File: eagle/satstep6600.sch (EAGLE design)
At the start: 42 parts, among them J3 STEPPER_CONN_2, T1 10K, U1 74HC123D

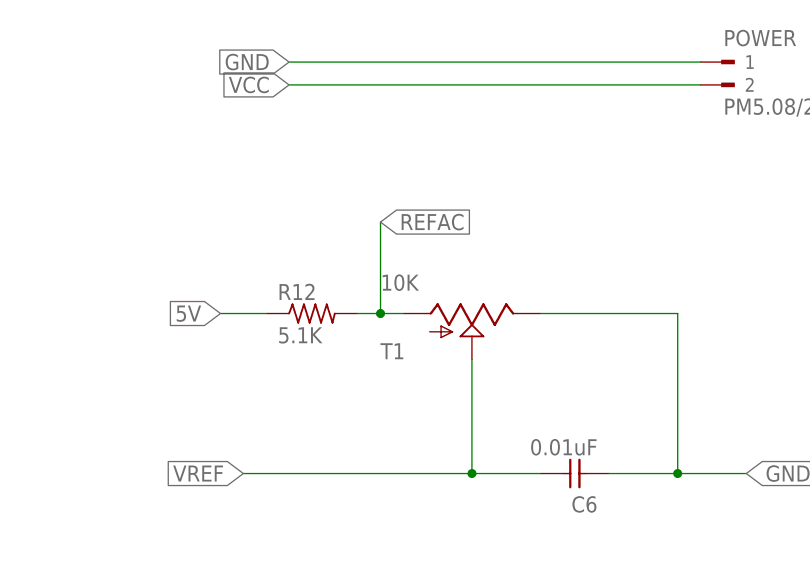
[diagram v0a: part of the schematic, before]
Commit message: mod the trimmmer value
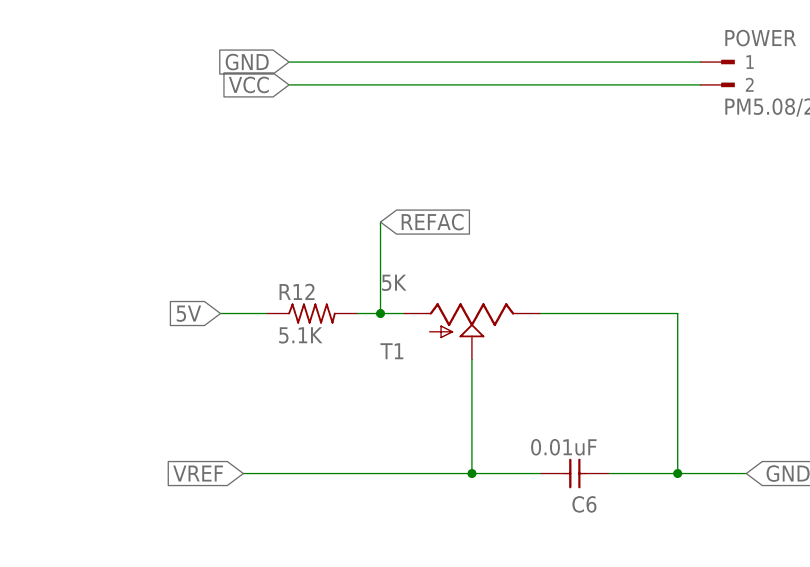
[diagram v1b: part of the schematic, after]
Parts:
- T1: value 10K -> 5K
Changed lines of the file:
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@@
 <?xml version="1.0" encoding="utf-8"?>
 <!DOCTYPE eagle SYSTEM "eagle.dtd">
-<eagle version="7.7.0">
+<eagle version="8.4.3">
 <drawing>
 <settings>
 <setting alwaysvectorfont="no"/>
+<setting keepoldvectorfont="yes"/>
 <setting verticaltext="up"/>
 </settings>
@@
 <part name="C6" library="FAB_Hello" deviceset="UNPOLARIZED_CAPACITOR" device="1206" value="0.01uF"/>
 <part name="R12" library="fab" deviceset="RES-US" device="1206" value="5.1K"/>
-<part name="T1" library="Ava" deviceset="TS53YL104MR10-TRIMMER" device="" value="10K"/>
+<part name="T1" library="Ava" deviceset="TS53YL104MR10-TRIMMER" device="" value="5K"/>
 <part name="U1" library="74HC123D" deviceset="74HC123D" device=""/>
 <part name="R13" library="fab" deviceset="RES-US" device="1206" value="5.1K"/>

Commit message: safier trimmer value
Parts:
- T1: value 5K -> 5k
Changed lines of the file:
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@@
 <part name="C6" library="FAB_Hello" deviceset="UNPOLARIZED_CAPACITOR" device="1206" value="0.01uF"/>
 <part name="R12" library="fab" deviceset="RES-US" device="1206" value="5.1K"/>
-<part name="T1" library="Ava" deviceset="TS53YL104MR10-TRIMMER" device="" value="5K"/>
+<part name="T1" library="Ava" deviceset="TS53YL104MR10-TRIMMER" device="" value="5k"/>
 <part name="U1" library="74HC123D" deviceset="74HC123D" device=""/>
 <part name="R13" library="fab" deviceset="RES-US" device="1206" value="5.1K"/>

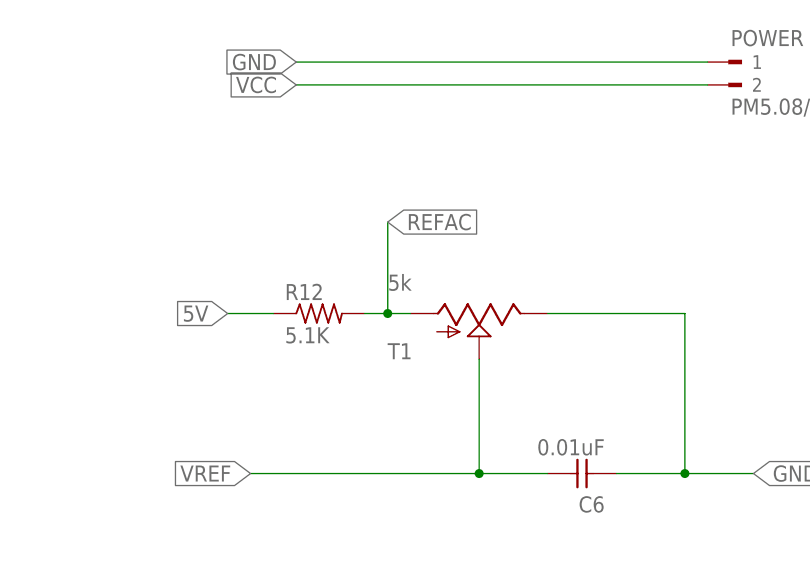
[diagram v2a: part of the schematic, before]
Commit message: safer trimmer value
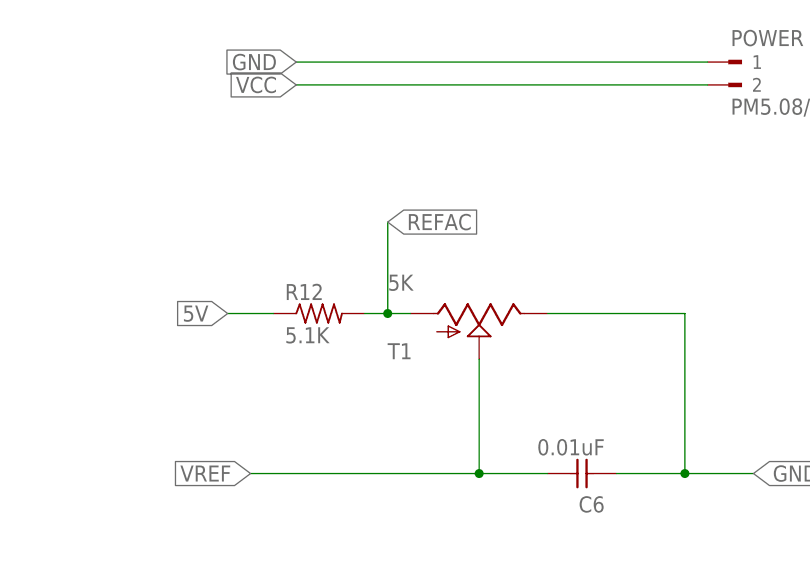
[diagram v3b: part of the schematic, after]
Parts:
- T1: value 5k -> 5K
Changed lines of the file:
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@@
 <part name="C6" library="FAB_Hello" deviceset="UNPOLARIZED_CAPACITOR" device="1206" value="0.01uF"/>
 <part name="R12" library="fab" deviceset="RES-US" device="1206" value="5.1K"/>
-<part name="T1" library="Ava" deviceset="TS53YL104MR10-TRIMMER" device="" value="5k"/>
+<part name="T1" library="Ava" deviceset="TS53YL104MR10-TRIMMER" device="" value="5K"/>
 <part name="U1" library="74HC123D" deviceset="74HC123D" device=""/>
 <part name="R13" library="fab" deviceset="RES-US" device="1206" value="5.1K"/>
